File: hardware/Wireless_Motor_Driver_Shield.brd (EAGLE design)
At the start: 59.7 x 53.3 mm, 97 parts, among them J1 5.5x2.1mm Barrel, Q1 MOSFET-NCHANNELBSS138, Q2 MOSFET-NCHANNELBSS138, Q3 MMBT2222A, Q4 DMG2307L, Q5 DMG2307L, Q6 DMG2307L, U1 XBEE-1XBEE-1_LOCK, U2 ARDUINO, U3 TB6612FNG

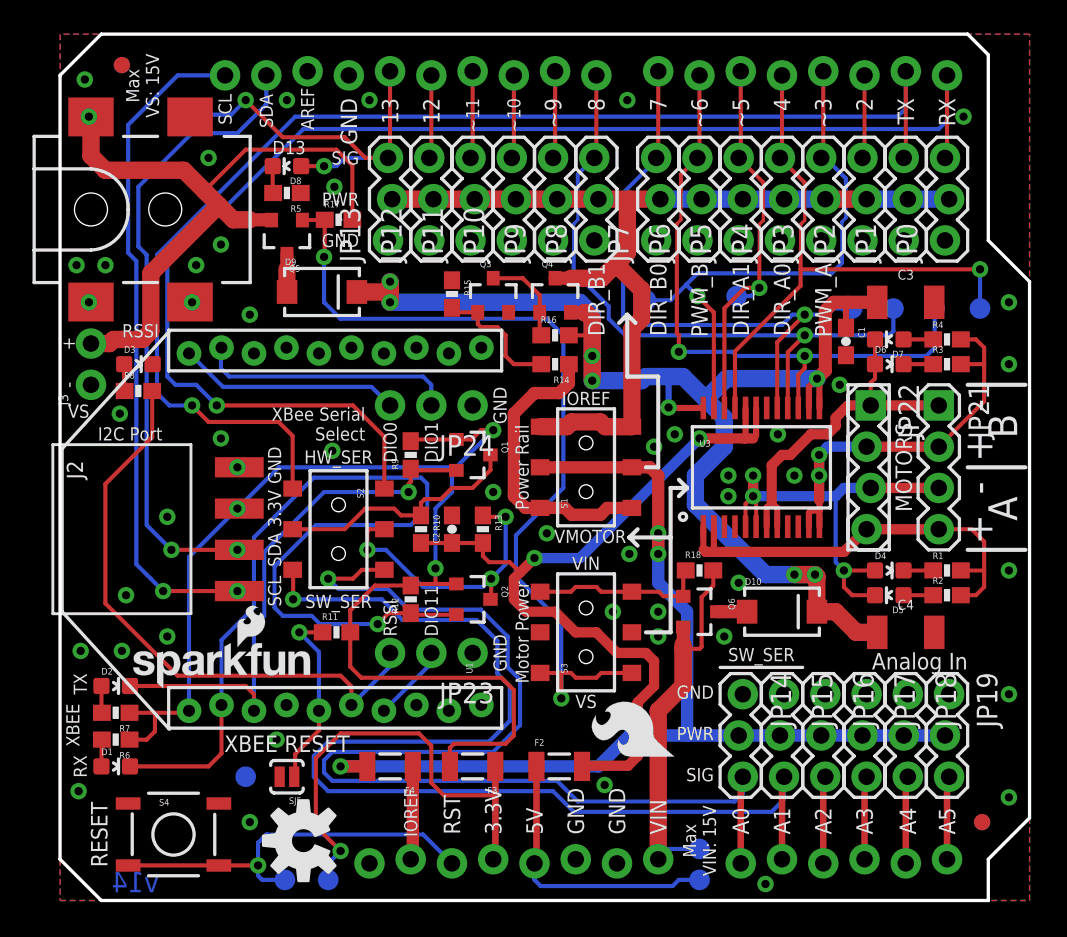
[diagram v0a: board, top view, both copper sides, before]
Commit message: Updated LED, RES, and CAP libraries to remove silk under parts
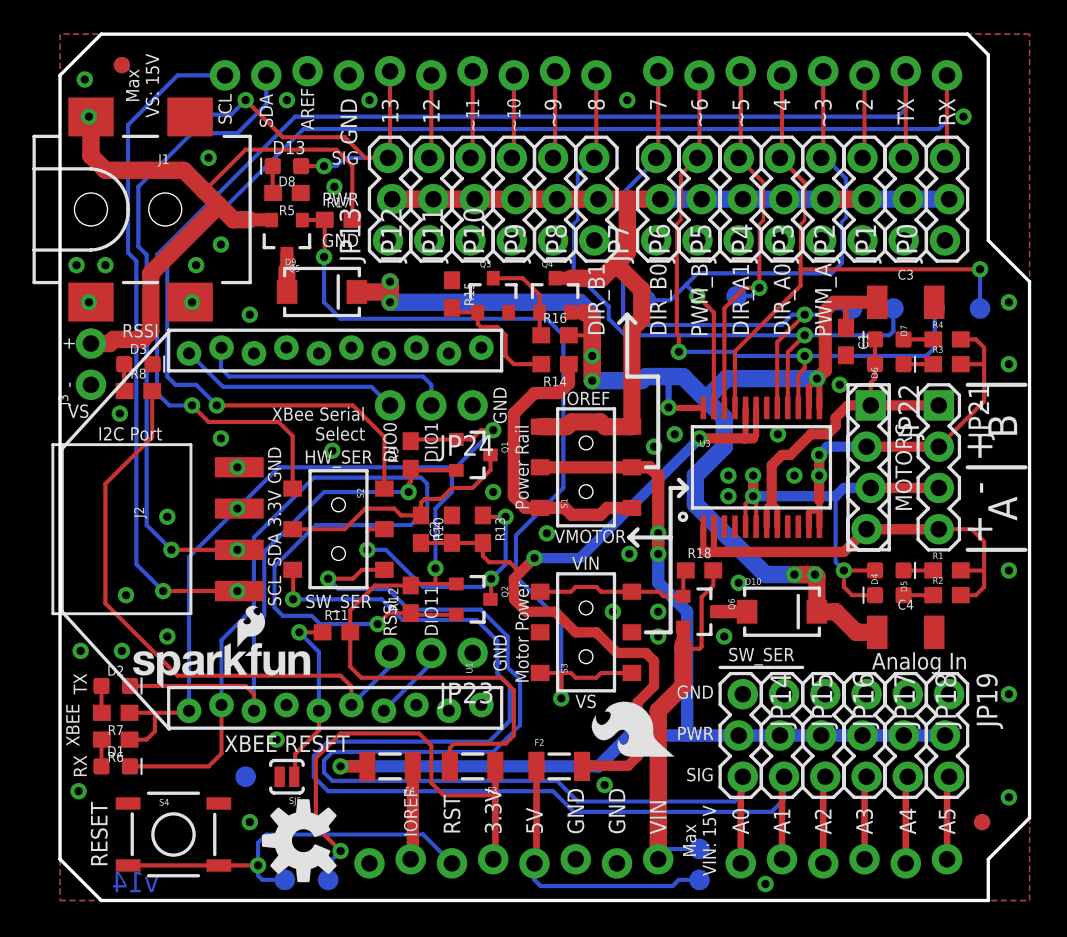
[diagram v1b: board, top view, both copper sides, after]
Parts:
- C1, C2: device SparkFun-Capacitors:0603-CAP -> SparkFun-Capacitors:0603
- D4, D6: value Blue -> BLUE
- JP21: device SparkFun-Connectors:1X04 -> SparkFun-Connectors:1X04@1
- JP22: device SparkFun-Connectors:1X04_LOCK -> SparkFun-Connectors:1X04_LOCK@1
- R1, R10, R11, R12, R13, R14, R2, R3, R4, R6, R7, R8, R9: value 1K -> 1k; device SparkFun-Resistors:0603-RES -> SparkFun-Resistors:0603
- R15, R16, R17, R18: value 10K -> 10k; device SparkFun-Resistors:0603-RES -> SparkFun-Resistors:0603
- R5: device SparkFun-Resistors:0603-RES -> SparkFun-Resistors:0603
- turned D1 to 0 degrees
- turned D2 to 0 degrees
- turned D3 to 0 degrees
- turned D4 to 0 degrees
- turned D5 to 180 degrees
- turned D6 to 0 degrees
- turned D7 to 180 degrees
- turned D8 to 180 degrees
